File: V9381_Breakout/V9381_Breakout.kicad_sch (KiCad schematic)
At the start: 13 parts, among them J1 Conn_01x10

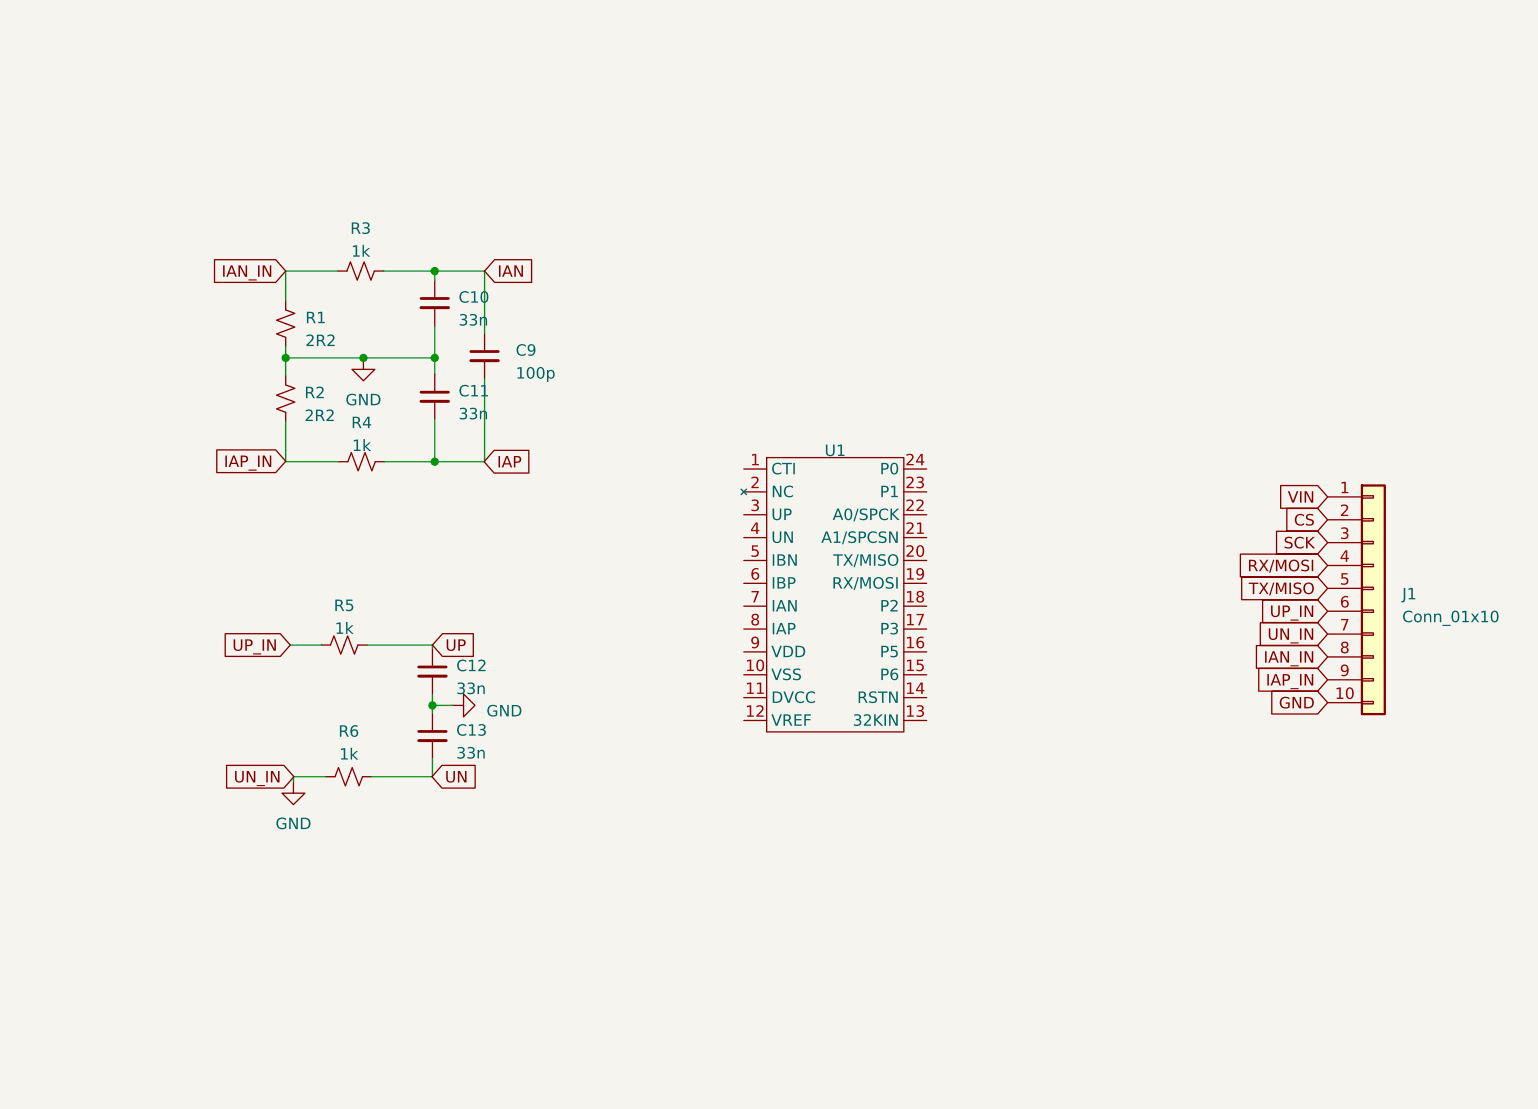
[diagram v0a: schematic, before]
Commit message: Start the wiring up and PCB outline
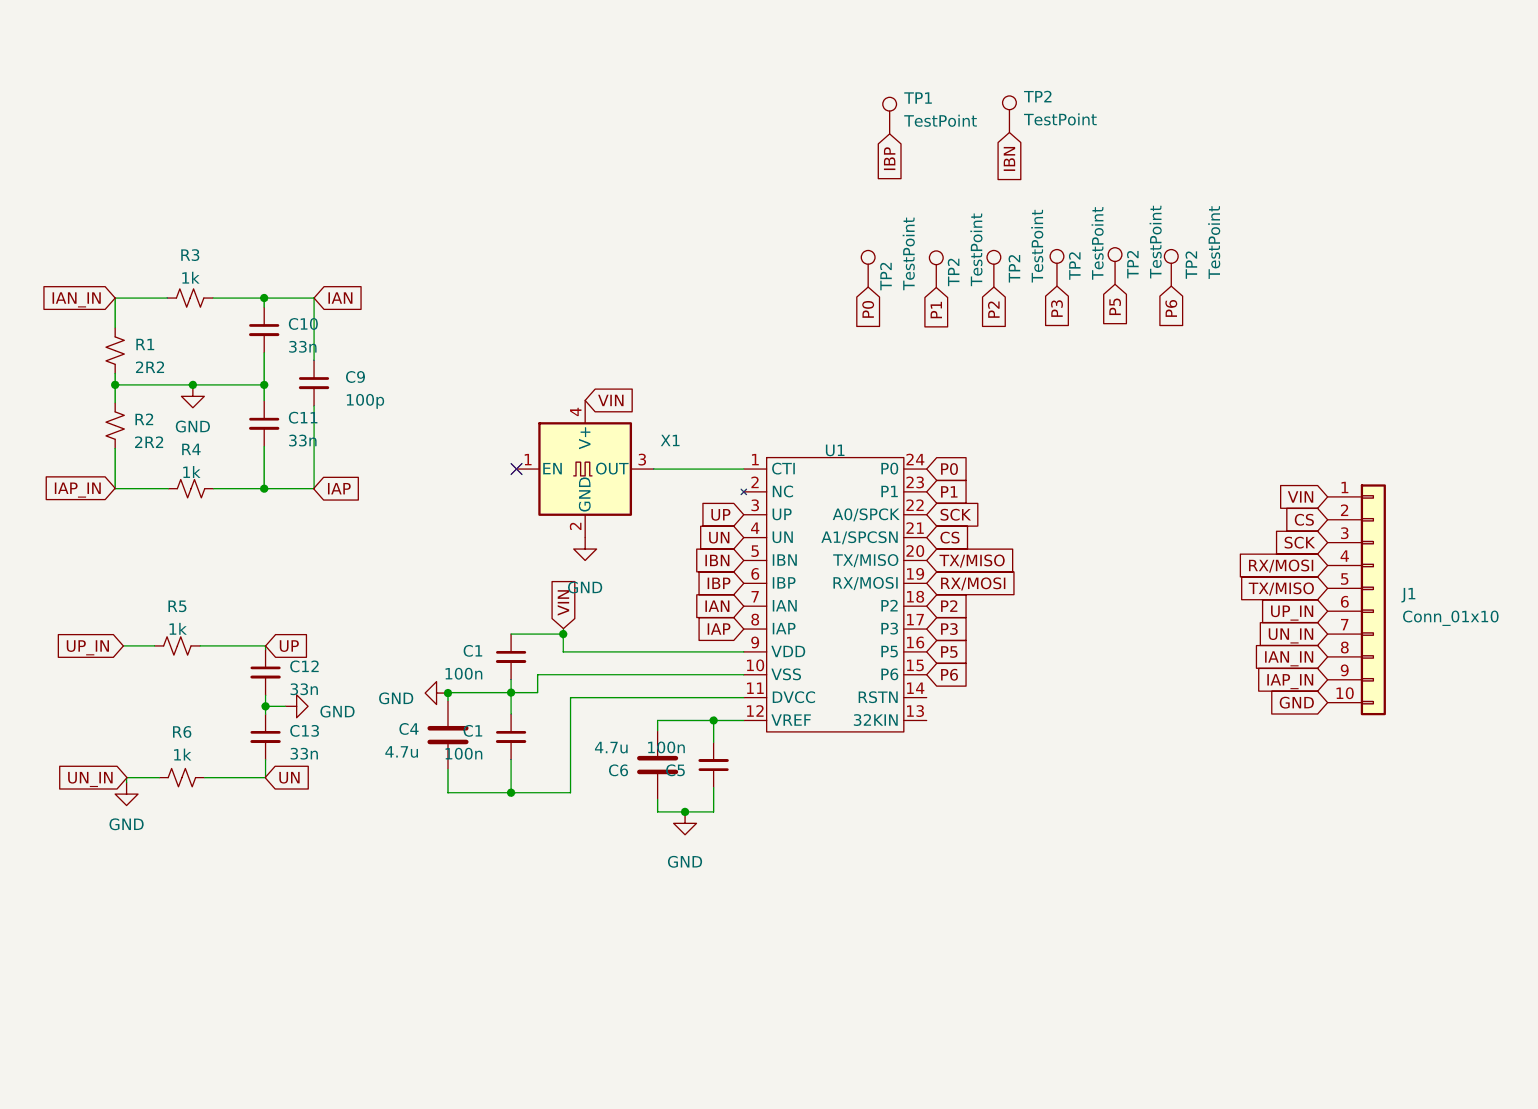
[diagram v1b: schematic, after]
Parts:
- added C1 (x2), C5: 100n, Capacitor_SMD:C_0603_1608Metric, symbol Device:C_Small
- added C4, C6: 4.7u, Capacitor_SMD:C_0805_2012Metric, symbol Device:C
- added TP1, TP2 (x7): TestPoint, TestPoint:TestPoint_Pad_1.5x1.5mm, symbol Connector:TestPoint
- added X1: XO32, Oscillator:Oscillator_SMD_EuroQuartz_XO32-4Pin_3.2x2.5mm, symbol Oscillator:XO32
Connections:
- net CS: now also U1.21 (A1/SPCSN)
- net GND: now also U1.10 (VSS), C1.1, C1.2, C4.1, C5.1, C6.1, X1.2 (GND)
- net IAN: now also U1.7 (IAN)
- net IAP: now also U1.8 (IAP)
- net RX/MOSI: now also U1.19 (RX/MOSI)
- net SCK: now also U1.22 (A0/SPCK)
- net TX/MISO: now also U1.20 (TX/MISO)
- net UN: now also U1.4 (UN)
- net UP: now also U1.3 (UP)
- net VIN: now also U1.9 (VDD), C1.1, X1.4 (V+)
- net at U1.1 (CTI): now also X1.3 (OUT)
- net at U1.11 (DVCC): now also C1.2, C4.2
- net at U1.12 (VREF): now also C5.2, C6.2
- net P6: now reaches U1.15 (P6)
- net P6: now also TP2.1
- net P5: now reaches U1.16 (P5)
- net P5: now also TP2.1
- net P3: now reaches U1.17 (P3)
- net P3: now also TP2.1
- net P2: now reaches U1.18 (P2)
- net P2: now also TP2.1
- net P1: now reaches U1.23 (P1)
- net P1: now also TP2.1
- net P0: now reaches U1.24 (P0)
- net P0: now also TP2.1
- net IBN: now reaches U1.5 (IBN)
- net IBN: now also TP2.1
- net IBP: now reaches U1.6 (IBP)
- net IBP: now also TP1.1
- no-connect marks 0 -> 1
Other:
- moved on the sheet: C10, C11, C12, C13, C9, R1, R2, R3, R4, R5, R6

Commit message: Finish routing
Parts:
- added TP2 (x2): TestPoint, TestPoint:TestPoint_Pad_1.5x1.5mm, symbol Connector:TestPoint
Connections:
- net 32KIN: now reaches U1.13 (32KIN)
- net 32KIN: now also TP2.1
- net ~{RST}: now reaches U1.14 (RSTN)
- net ~{RST}: now also TP2.1
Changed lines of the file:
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@@
+    )
+  )
+  (global_label "~{RST}" (shape input) (at 144.9832 103.632 0) (fields_autoplaced)
+    (effects (font (size 1.27 1.27)) (justify left))
+    (property "Intersheetrefs" "${INTERSHEET_REFS}" (at 151.4155 103.632 0)
+      (effects (font (size 1.27 1.27)) (justify left) hide)
+    )
+  )
+  (global_label "32KIN" (shape input) (at 144.9832 106.172 0) (fields_autoplaced)
+    (effects (font (size 1.27 1.27)) (justify left))
+    (property "Intersheetrefs" "${INTERSHEET_REFS}" (at 153.5927 106.172 0)
+      (effects (font (size 1.27 1.27)) (justify left) hide)
     )
   )
@@
     )
   )
+  (global_label "32KIN" (shape input) (at 177.1396 39.9796 270) (fields_autoplaced)
+    (effects (font (size 1.27 1.27)) (justify right))
+    (property "Intersheetrefs" "${INTERSHEET_REFS}" (at 177.1396 48.5891 90)
+      (effects (font (size 1.27 1.27)) (justify right) hide)
+    )
+  )
   (global_label "IAN_IN" (shape input) (at 54.8132 59.2328 180) (fields_autoplaced)
     (effects (font (size 1.27 1.27)) (justify right))
@@
     (property "Intersheetrefs" "${INTERSHEET_REFS}" (at 104.6226 90.0315 90)
       (effects (font (size 1.27 1.27)) (justify left) hide)
+    )
+  )
+  (global_label "~{RST}" (shape input) (at 169.037 40.1828 270) (fields_autoplaced)
+    (effects (font (size 1.27 1.27)) (justify right))
+    (property "Intersheetrefs" "${INTERSHEET_REFS}" (at 169.037 46.6151 90)
+      (effects (font (size 1.27 1.27)) (justify right) hide)
     )
   )
@@
         (path "/891e2995-ecf8-4e0a-82a0-40782119b9b2"
           (reference "TP8") (unit 1)
+        )
+      )
+      (project "V9360_Breakout"
+        (path "/f6ffeb9c-2174-49f8-b838-c33315c45e1a"
+          (reference "TP2") (unit 1)
+        )
+      )
+    )
+  )
+  (symbol (lib_id "Connector:TestPoint") (at 177.1396 39.9796 0) (unit 1)
+    (in_bom yes) (on_board yes) (dnp no)
+    (property "Reference" "TP2" (at 179.0954 39.6494 90)
+      (effects (font (size 1.27 1.27)) (justify left))
+    )
+    (property "Value" "TestPoint" (at 181.6354 39.6494 90)
+      (effects (font (size 1.27 1.27)) (justify left))
+    )
+    (property "Footprint" "TestPoint:TestPoint_Pad_1.5x1.5mm" (at 182.2196 39.9796 0)
+      (effects (font (size 1.27 1.27)) hide)
+    )
+    (property "Datasheet" "~" (at 182.2196 39.9796 0)
+      (effects (font (size 1.27 1.27)) hide)
+    )
+    (property "DNP" "..." (at 177.1396 39.9796 0)
+      (effects (font (size 1.27 1.27)) hide)
+    )
+    (property "MPN" "" (at 177.1396 39.9796 0)
+      (effects (font (size 1.27 1.27)) hide)
+    )
+    (pin "1")
+    (instances
+      (project "V9261F_Breakout"
+        (path "/5aeaad9e-9db0-42b8-ae2b-aea1c149c881"
+          (reference "TP2") (unit 1)
+        )
+      )
+      (project "V9381_Breakout"
+        (path "/891e2995-ecf8-4e0a-82a0-40782119b9b2"
+          (reference "TP10") (unit 1)
         )
       )
@@
         )
       )
+    )
+  )
+  (symbol (lib_id "Connector:TestPoint") (at 169.037 40.1828 0) (unit 1)
+    (in_bom yes) (on_board yes) (dnp no)
+    (property "Reference" "TP2" (at 171.2976 39.2938 90)
+      (effects (font (size 1.27 1.27)) (justify left))
+    )
+    (property "Value" "TestPoint" (at 173.8376 39.2938 90)
+      (effects (font (size 1.27 1.27)) (justify left))
+    )
+    (property "Footprint" "TestPoint:TestPoint_Pad_1.5x1.5mm" (at 174.117 40.1828 0)
+      (effects (font (size 1.27 1.27)) hide)
+    )
+    (property "Datasheet" "~" (at 174.117 40.1828 0)
+      (effects (font (size 1.27 1.27)) hide)
+    )
+    (property "DNP" "..." (at 169.037 40.1828 0)
+      (effects (font (size 1.27 1.27)) hide)
+    )
+    (property "MPN" "" (at 169.037 40.1828 0)
+      (effects (font (size 1.27 1.27)) hide)
+    )
+    (pin "1")
+    (instances
+      (project "V9261F_Breakout"
+        (path "/5aeaad9e-9db0-42b8-ae2b-aea1c149c881"
+          (reference "TP2") (unit 1)
+        )
+      )
+      (project "V9381_Breakout"
+        (path "/891e2995-ecf8-4e0a-82a0-40782119b9b2"
+          (reference "TP9") (unit 1)
+        )
+      )
+      (project "V9360_Breakout"
+        (path "/f6ffeb9c-2174-49f8-b838-c33315c45e1a"
+          (reference "TP2") (unit 1)
+        )
+      )

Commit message: Finish routing and create fab outputs
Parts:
- added SYM1: Logo_Open_Hardware_Small, Symbol:OSHW-Logo2_9.8x8mm_SilkScreen, symbol Graphic:Logo_Open_Hardware_Small
- U1: value ~ -> V9381; MPN (none) -> V9381
- X1: MPN (none) -> SX3M6.5536B20F30TNN
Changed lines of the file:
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@@
+      (effects (font (size 1.27 1.27)) hide)
+    )
+    (property "MPN" "SX3M6.5536B20F30TNN" (at 107.0356 78.232 0)
       (effects (font (size 1.27 1.27)) hide)
     )
@@
     )
   )
+  (symbol (lib_id "Graphic:Logo_Open_Hardware_Small") (at 131.064 143.002 0) (unit 1)
+    (in_bom no) (on_board yes) (dnp no) (fields_autoplaced)
+    (property "Reference" "SYM1" (at 131.064 136.017 0)
+      (effects (font (size 1.27 1.27)) hide)
+    )
+    (property "Value" "Logo_Open_Hardware_Small" (at 131.064 148.717 0)
+      (effects (font (size 1.27 1.27)) hide)
+    )
+    (property "Footprint" "Symbol:OSHW-Logo2_9.8x8mm_SilkScreen" (at 131.064 143.002 0)
+      (effects (font (size 1.27 1.27)) hide)
+    )
+    (property "Datasheet" "~" (at 131.064 143.002 0)
+      (effects (font (size 1.27 1.27)) hide)
+    )
+    (property "Sim.Enable" "0" (at 131.064 143.002 0)
+      (effects (font (size 1.27 1.27)) hide)
+    )
+    (property "DNP" "..." (at 131.064 143.002 0)
+      (effects (font (size 1.27 1.27)) hide)
+    )
+    (property "MPN" "" (at 131.064 143.002 0)
+      (effects (font (size 1.27 1.27)) hide)
+    )
+    (instances
+      (project "V9381_Breakout"
+        (path "/891e2995-ecf8-4e0a-82a0-40782119b9b2"
+          (reference "SYM1") (unit 1)
+        )
+      )
+      (project "V9360_Breakout"
+        (path "/f6ffeb9c-2174-49f8-b838-c33315c45e1a"
+          (reference "SYM1") (unit 1)
+        )
+      )
+    )
+  )
   (symbol (lib_id "Connector:TestPoint") (at 165.9128 57.7088 0) (unit 1)
     (in_bom yes) (on_board yes) (dnp no)
@@
       (effects (font (size 1.27 1.27)))
     )
-    (property "Value" "~" (at 134.8232 74.422 0)
+    (property "Value" "V9381" (at 134.8232 74.422 0)
       (effects (font (size 1.27 1.27)))
     )
@@
       (effects (font (size 1.27 1.27)) hide)
     )
+    (property "MPN" "V9381" (at 134.8232 74.422 0)
+      (effects (font (size 1.27 1.27)) hide)
+    )
